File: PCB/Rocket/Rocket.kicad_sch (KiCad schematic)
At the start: 36 parts, among them J1 Conn_01x08_Pin, J2 Conn_01x04_Pin, J3 Conn_01x07_Pin, J4 Micro_SD_Card, J5 Conn_ARM_JTAG_SWD_10, J6 Conn_01x04_Pin, J7 1987724, SW1 CK_KMS2xxG, SW2 CK_KMS2xxG, U1 STM32L476RGTx, U2 MC78L05ACDR2G, U3 MIC5365-3.3YC5-TR

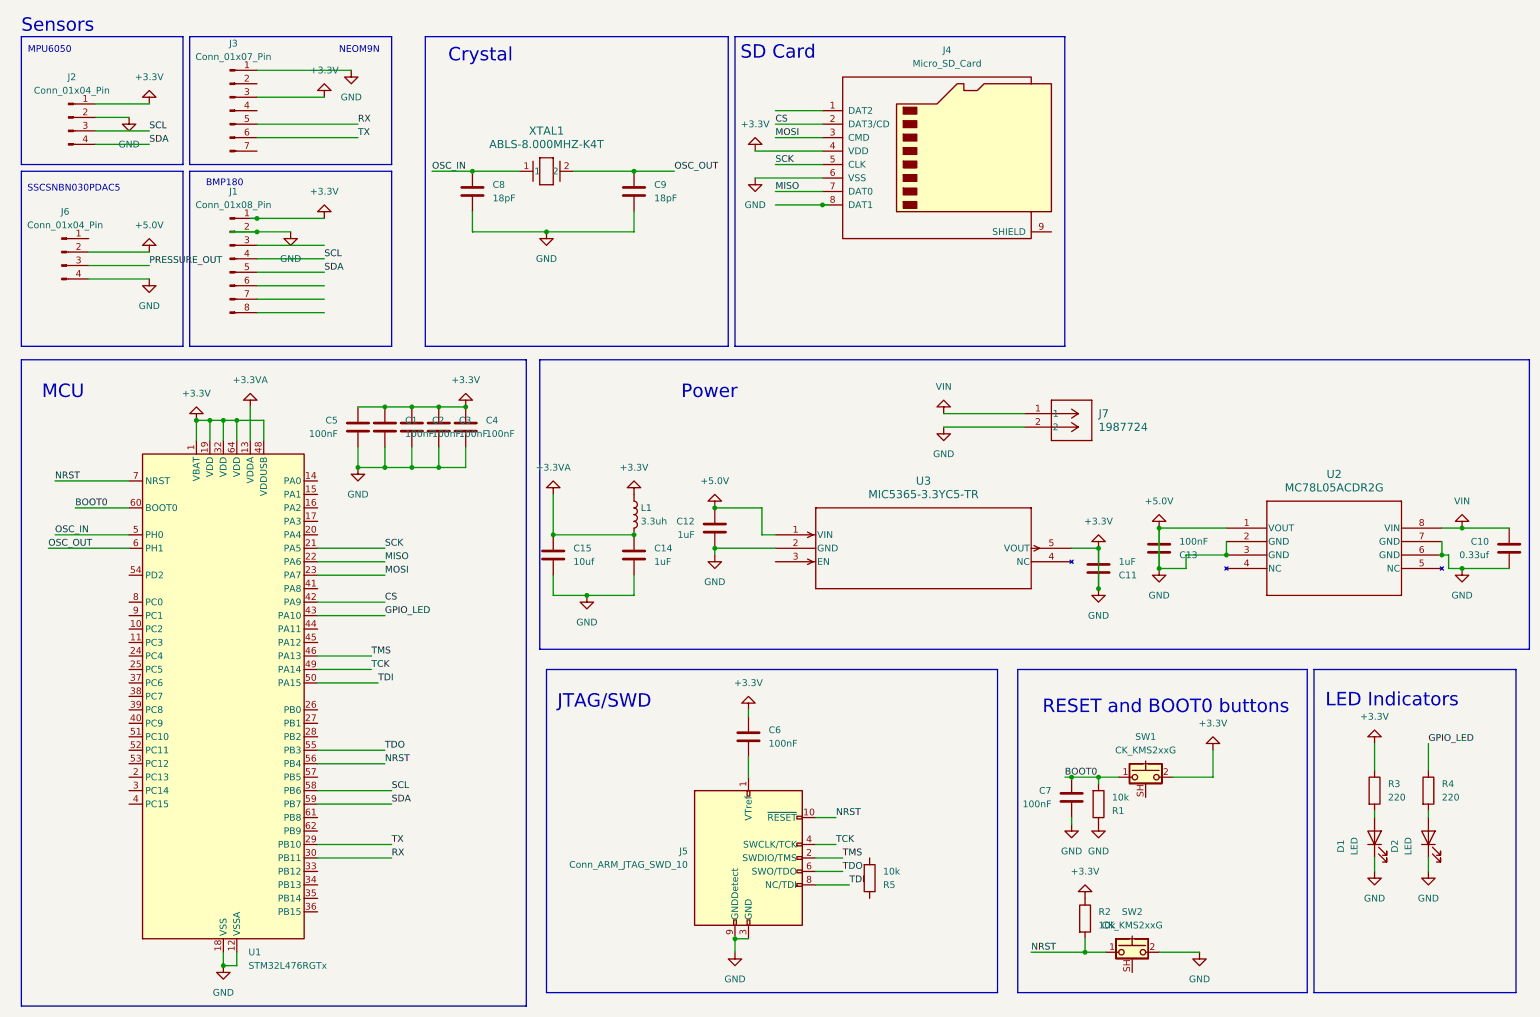
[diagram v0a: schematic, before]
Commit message: Added ESD protection for SD card and pull up resistors.
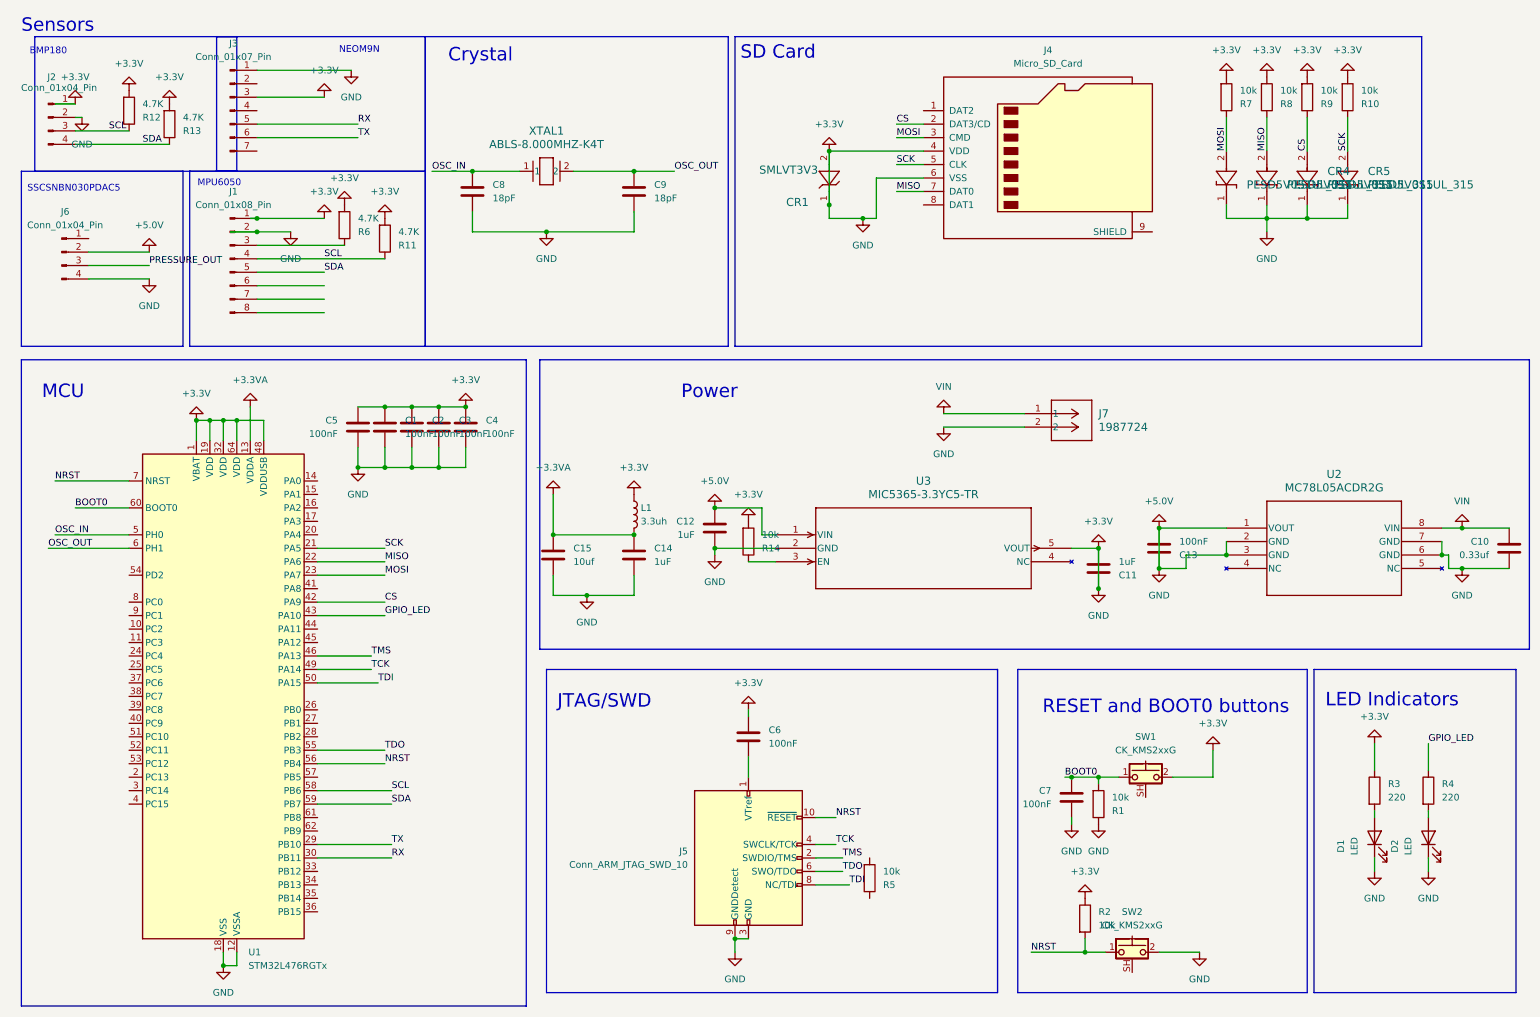
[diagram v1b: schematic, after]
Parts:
- added CR1: SMLVT3V3, SMB_STM, symbol 2025-01-22_04-11-48:SMLVT3V3
- added CR2, CR3, CR4, CR5: PESD5V0S1UL_315, DFN1006-2_SOD882_NEX, symbol PESD5V0S1UL,315:PESD5V0S1UL_315
- added R10, R14, R7, R8, R9: 10k, Resistor_SMD:R_0201_0603Metric_Pad0.64x0.40mm_HandSolder, symbol Device:R
- added R11, R12, R13, R6: 4.7K, Resistor_SMD:R_0201_0603Metric_Pad0.64x0.40mm_HandSolder, symbol Device:R
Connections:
- net +3.3V: now also CR1.1, CR1.2, CR2.1, CR3.1, CR4.1, CR5.1, R10.2, R11.2, R12.2, R13.2, R14.2, R6.2, R7.2, R8.2, R9.2
- net CS: now also CR4.2, R9.1
- net MISO: now also CR3.2, R8.1
- net MOSI: now also CR2.2, R7.1
- net SCK: now also CR5.2, R10.1
- net SCL: now also R11.1, R12.1
- net SDA: now also R13.1
- net at J1.3 (Pin_3): now also R6.1
- net at U3.3 (EN): now also R14.1
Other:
- moved on the sheet: J2, J4

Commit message: Updated layout.
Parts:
- removed R11, R6: 4.7K, Resistor_SMD:R_0201_0603Metric_Pad0.64x0.40mm_HandSolder, symbol Device:R
- removed R5: 10k, Resistor_SMD:R_0201_0603Metric_Pad0.64x0.40mm_HandSolder, symbol Device:R
- CR1: footprint SMB_STM -> SMLVT3V3:SMB_STM
- CR2, CR3, CR4, CR5: footprint DFN1006-2_SOD882_NEX -> PESD5V0S1UL,315:DFN1006-2_SOD882_NEX
- D1, D2: footprint (none) -> LED_SMD:LED_0603_1608Metric
- L1: footprint (none) -> Inductor_SMD:L_0201_0603Metric
- U2: footprint SOIC8_ONS -> MC78L05ACDR2G:SOIC8_ONS
- U3: footprint SC-70_C5_MCH -> MIC5365-3.3YC5-TR:SC-70_C5_MCH
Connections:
- net +3.3V: no longer C1.2, C10.2, C11.1, C12.1, C12.2, C13.1, C13.2, C14.2, C15.2, C2.2, C3.2, C4.2, C5.2, C6.1, C7.2, C8.2, C9.2, CR1.1, CR2.1, CR3.1, CR4.1, CR5.1, D1.1 (K), D2.1 (K), J1.2 (Pin_2), J2.2 (Pin_2), J3.1 (Pin_1), J4.6 (VSS), J5.3 (GND), J5.5 (GND), J5.9 (GNDDetect), J6.2 (Pin_2), J6.4 (Pin_4), J7.2, R1.1, SW2.2, U1.12 (VSSA), U1.18 (VSS), U1.31 (VSS), U1.47 (VSS), U1.63 (VSS), U2.1 (VOUT), U2.2 (GND), U2.3 (GND), U2.6 (GND), U2.7 (GND), U3.1 (VIN), U3.2 (GND)
- net +3.3VA: now also C6.1
- net CS: now also U1.20 (PA4); no longer U1.42 (PA9)
- net PRESSURE_OUT: now also U1.16 (PA2)
- net SCL: now also J1.3 (Pin_3); no longer J1.4 (Pin_4)
- net SDA: now also J1.4 (Pin_4); no longer J1.5 (Pin_5)
- net VIN renamed +VDC
- new net +5V: C12.1, C13.2, J6.2 (Pin_2), U2.1 (VOUT), U3.1 (VIN)
- new net GND: C1.2, C10.2, C11.1, C12.2, C13.1, C14.2, C15.2, C2.2, C3.2, C4.2, C5.2, C7.2, C8.2, C9.2, CR1.1, CR2.1, CR3.1, CR4.1, CR5.1, D1.1 (K), D2.1 (K), J1.2 (Pin_2), J2.2 (Pin_2), J3.1 (Pin_1), J4.6 (VSS), J5.3 (GND), J5.5 (GND), J5.9 (GNDDetect), J6.4 (Pin_4), J7.2, R1.1, SW2.2, U1.12 (VSSA), U1.18 (VSS), U1.31 (VSS), U1.47 (VSS), U1.63 (VSS), U2.2 (GND), U2.3 (GND), U2.6 (GND), U2.7 (GND), U3.2 (GND)

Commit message: Fixing DRC errors.
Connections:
- net NRST: no longer U1.56 (PB4)
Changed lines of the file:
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@@
 	)
 	(label "NRST"
-		(at 82.55 153.67 0)
-		(fields_autoplaced yes)
-		(effects
-			(font
-				(size 1.27 1.27)
-			)
-			(justify left bottom)
-		)
-	)
-	(label "NRST"
 		(at 167.64 163.83 0)
 		(fields_autoplaced yes)
@@
 					(size 1.27 1.27)
 				)
+				(hide yes)
 			)
 		)
@@
 				)
 				(justify left)
+				(hide yes)
 			)
 		)
@@
 					(size 1.27 1.27)
 				)
+				(hide yes)
 			)
 		)
@@
 					(size 1.27 1.27)
 				)
+				(hide yes)
 			)
 		)
@@
 					(size 1.27 1.27)
 				)
+				(hide yes)
 			)
 		)

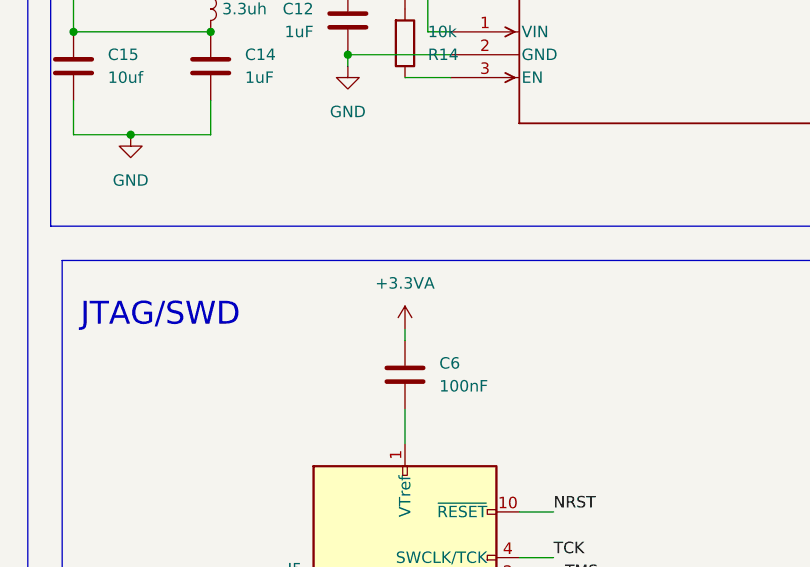
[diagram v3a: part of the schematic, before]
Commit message: Removed all DRC errors.
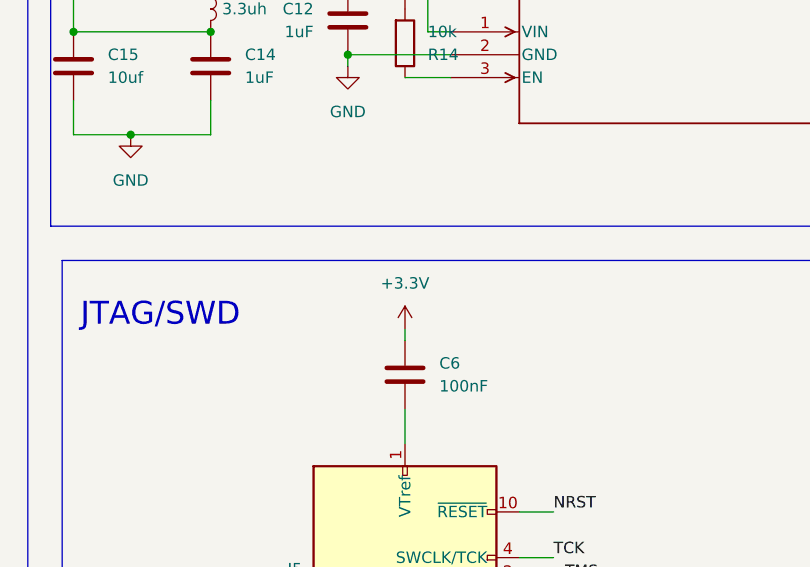
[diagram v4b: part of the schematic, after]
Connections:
- net +3.3V: now also C6.1
- net +3.3VA: no longer C6.1
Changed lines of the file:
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@@
-	)
-	(symbol
-		(lib_id "power:+3.3VA")
-		(at 151.13 143.51 0)
-		(unit 1)
-		(exclude_from_sim no)
-		(in_bom yes)
-		(on_board yes)
-		(dnp no)
-		(fields_autoplaced yes)
-		(property "Reference" "#PWR036"
-			(at 151.13 147.32 0)
-			(effects
-				(font
-					(size 1.27 1.27)
-				)
-				(hide yes)
-			)
-		)
-		(property "Value" "+3.3VA"
-			(at 151.13 138.43 0)
-			(effects
-				(font
-					(size 1.27 1.27)
-				)
-			)
-		)
-		(property "Footprint" ""
-			(at 151.13 143.51 0)
-			(effects
-				(font
-					(size 1.27 1.27)
-				)
-				(hide yes)
-			)
-		)
-		(property "Datasheet" ""
-			(at 151.13 143.51 0)
-			(effects
-				(font
-					(size 1.27 1.27)
-				)
-				(hide yes)
-			)
-		)
-		(property "Description" "Power symbol creates a global label with name \"+3.3VA\""
-			(at 151.13 143.51 0)
-			(effects
-				(font
-					(size 1.27 1.27)
-				)
-				(hide yes)
-			)
-		)
-		(pin "1"
-		)
-		(instances
-			(project "Rocket"
-				(path "/5dfb71dd-d286-4e20-8826-e4e4d6e6f930"
-					(reference "#PWR036")
-					(unit 1)
-				)
-			)
-		)
 	)
 	(symbol
@@
 					(unit 1)
 				)
+			)
+		)
+	)
+	(symbol
+		(lib_id "power:+3.3V")
+		(at 151.13 143.51 0)
+		(unit 1)
+		(exclude_from_sim no)
+		(in_bom yes)
+		(on_board yes)
+		(dnp no)
+		(fields_autoplaced yes)
+		(property "Reference" "#PWR036"
+			(at 151.13 147.32 0)
+			(effects
+				(font
+					(size 1.27 1.27)
+				)
+				(hide yes)
+			)
+		)
+		(property "Value" "+3.3V"
+			(at 151.13 138.43 0)
+			(effects
+				(font
+					(size 1.27 1.27)
+				)
+			)
+		)
+		(property "Footprint" ""
+			(at 151.13 143.51 0)
+			(effects
+				(font
+					(size 1.27 1.27)
+				)
+				(hide yes)
+			)
+		)
+		(property "Datasheet" ""
+			(at 151.13 143.51 0)
+			(effects
+				(font
+					(size 1.27 1.27)
+				)
+				(hide yes)
+			)
+		)
+		(property "Description" "Power symbol creates a global label with name \"+3.3V\""
+			(at 151.13 143.51 0)
+			(effects
+				(font
+					(size 1.27 1.27)
+				)
+				(hide yes)
+			)
+		)
+		(pin "1"
+		)
+		(instances
+			(project "Rocket"
+				(path "/5dfb71dd-d286-4e20-8826-e4e4d6e6f930"
+					(reference "#PWR036")
+					(unit 1)
+				)
